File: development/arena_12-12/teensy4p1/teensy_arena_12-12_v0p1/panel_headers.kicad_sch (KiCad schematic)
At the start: 27 parts, among them P1 CONN15, P10 CONN15, P11 CONN15, P12 CONN15, P2 CONN15, P3 CONN15, P4 CONN15, P5 CONN15, P6 CONN15, P7 CONN15, P8 CONN15, P9 CONN15, Q2 MOSFET_NCHAN

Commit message: Worked on 12-12 teensy4p1 arena without vreg.
Modified SPI connections from teensy to panel columns so that all
signals go from a single source to a single destinatin. Also, added
source termination resistors and schmitt trigger buffers to all SPI
signals.
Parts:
- added C100, C101, C102, C103, C104, C105, C106, C107, C108, C109, C110, C111, C112, C113, C114, C115, C116, C117, C118, C119, C120, C121, C122, C123, C124, C125, C126, C127, C128, C129, C130, C131, C132, C133, C134, C135, C136, C137, C138, C139, C140, C141, C142, C143, C144, C145, C146, C147, C148, C149, C150, C151, C152, C153, C154, C155, C156, C157, C158, C159, C160, C161, C162, C163, C164, C165, C166, C167, C168, C169, C170, C171, C172, C77, C78, C79, C80, C81, C82, C83, C84, C85, C86, C87, C88, C89, C90, C91, C92, C93, C94, C95, C96, C97, C98, C99: 0.1uF, Capacitor_SMD:C_0603_1608Metric, symbol Device:C
- added R127, R128, R129, R130, R131, R132, R133, R134, R135, R136, R137, R138, R139, R140, R141, R142, R143, R144, R145, R146, R147, R148, R149, R150, R151, R152, R153, R154, R155, R156, R157, R158, R159, R160, R161, R162, R163, R164, R165, R166, R167, R168, R169, R170, R171, R172, R173, R174, R175, R176, R177, R178, R179, R180, R181, R182, R183, R184, R185, R186, R187, R188, R189, R190, R191, R192, R193, R194, R195, R196, R197, R198, R199, R200, R201, R202, R203, R204, R205, R206, R207, R208, R209, R210, R211, R212, R213, R214, R215, R216, R217, R218, R219, R220, R221, R222: 68, symbol Device:R
- added U100, U101, U102, U103, U104, U105, U106, U107, U108, U109, U110, U111, U112, U113, U114, U115, U116, U117, U118, U119, U120, U121, U122, U123, U124, U125, U126, U127, U128, U129, U130, U131, U132, U133, U134, U135, U136, U137, U138, U139, U140, U141, U142, U143, U144, U145, U146, U147, U148, U149, U54, U55, U56, U57, U58, U59, U60, U61, U62, U63, U64, U65, U66, U67, U68, U69, U70, U71, U72, U73, U74, U75, U76, U77, U78, U79, U80, U81, U82, U83, U84, U85, U86, U87, U88, U89, U90, U91, U92, U93, U94, U95, U96, U97, U98, U99: 74LVC1G17, symbol 74xGxx:74LVC1G17
- Q2: footprint Package_TO_SOT_SMD:SOT-23-3 -> (none)
- renumbered C11 to C65, C12 to C66, C13 to C67, C14 to C68, C15 to C69, C16 to C70, C17 to C71, C18 to C72, C19 to C73, C20 to C74, C21 to C75, C22 to C76
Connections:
- net +5V: now also C100.1, C101.1, C102.1, C103.1, C104.1, C105.1, C106.1, C107.1, C108.1, C109.1, C110.1, C111.1, C112.1, C113.1, C114.1, C115.1, C116.1, C117.1, C118.1, C119.1, C120.1, C121.1, C122.1, C123.1, C124.1, C125.1, C126.1, C127.1, C128.1, C129.1, C130.1, C131.1, C132.1, C133.1, C134.1, C135.1, C136.1, C137.1, C138.1, C139.1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
- net GND: now also C100.2, C101.2, C102.2, C103.2, C104.2, C105.2, C106.2, C107.2, C108.2, C109.2, C110.2, C111.2, C112.2, C113.2, C114.2, C115.2, C116.2, C117.2, C118.2, C119.2, C120.2, C121.2, C122.2, C123.2, C124.2, C125.2, C126.2, C127.2, C128.2, C129.2, C130.2, C131.2, C132.2, C133.2, C134.2, C135.2, C136.2, C137.2, C138.2, C139.2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
- net PAN5V.EXT_INT: now also U101.2, U109.2, U117.2, U125.2, U133.2, U141.2, U149.2, U61.2, U69.2, U77.2, U85.2, U93.2; no longer P1.15, P10.15, P11.15, P12.15, P2.15, P3.15, P4.15, P5.15, P6.15, P7.15, P8.15, P9.15
- net PAN5V.MISO_0: no longer P4.6
- net PAN5V.CS_00 renamed HDR_CS_00_P1
- net HDR_CS_00_P1: now also R129.1; no longer P7.7
- net PAN5V.CS_01 renamed HDR_CS_01_P1
- net HDR_CS_01_P1: now also R130.1; no longer P7.8
- net PAN5V.CS_02 renamed HDR_CS_02_P1
- net HDR_CS_02_P1: now also R131.1; no longer P7.9
- net PAN5V.CS_03 renamed HDR_CS_03_P1
- net HDR_CS_03_P1: now also R132.1; no longer P7.10
- net PAN5V.CS_04 renamed HDR_CS_04_P1
- net HDR_CS_04_P1: now also R133.1; no longer P7.11
- net PAN5V.CS_05 renamed HDR_CS_05_P2
- net HDR_CS_05_P2: now also R137.1; no longer P8.7
- net PAN5V.CS_06 renamed HDR_CS_06_P2
- net HDR_CS_06_P2: now also R138.1; no longer P8.8
- net PAN5V.CS_07 renamed HDR_CS_07_P2
- net HDR_CS_07_P2: now also R139.1; no longer P8.9
- net PAN5V.CS_08 renamed HDR_CS_08_P2
- net HDR_CS_08_P2: now also R140.1; no longer P8.10
- net PAN5V.CS_09 renamed HDR_CS_09_P2
- net HDR_CS_09_P2: now also R141.1; no longer P8.11
- net PAN5V.CS_10 renamed HDR_CS_10_P3
- net HDR_CS_10_P3: now also R145.1; no longer P9.7
- net PAN5V.CS_11 renamed HDR_CS_11_P3
- net HDR_CS_11_P3: now also R146.1; no longer P9.8
- net PAN5V.CS_12 renamed HDR_CS_12_P3
- net HDR_CS_12_P3: now also R147.1; no longer P9.9
- net PAN5V.CS_13 renamed HDR_CS_13_P3
- net HDR_CS_13_P3: now also R148.1; no longer P9.10
- net PAN5V.CS_14 renamed HDR_CS_14_P3
- net HDR_CS_14_P3: now also R149.1; no longer P9.11
- net PAN5V.CS_15 renamed HDR_CS_15_P10
- net HDR_CS_15_P10: now also R201.1; no longer P4.7
- net PAN5V.CS_16 renamed HDR_CS_16_P10
- net HDR_CS_16_P10: now also R202.1; no longer P4.8
- net PAN5V.CS_17 renamed HDR_CS_17_P10
- net HDR_CS_17_P10: now also R203.1; no longer P4.9
- net PAN5V.CS_18 renamed HDR_CS_18_P10
- net HDR_CS_18_P10: now also R204.1; no longer P4.10
- net PAN5V.CS_19 renamed HDR_CS_19_P10
- net HDR_CS_19_P10: now also R205.1; no longer P4.11
- net PAN5V.CS_20 renamed HDR_CS_20_P11
- net HDR_CS_20_P11: now also R209.1; no longer P5.7
- net PAN5V.CS_21 renamed HDR_CS_21_P11
- net HDR_CS_21_P11: now also R210.1; no longer P5.8
- net PAN5V.CS_22 renamed HDR_CS_22_P11
- net HDR_CS_22_P11: now also R211.1; no longer P5.9
- net PAN5V.CS_23 renamed HDR_CS_23_P11
- net HDR_CS_23_P11: now also R212.1; no longer P5.10
- net PAN5V.CS_24 renamed HDR_CS_24_P11
- net HDR_CS_24_P11: now also R213.1; no longer P5.11
- net PAN5V.CS_25 renamed HDR_CS_25_P12
- net HDR_CS_25_P12: now also R217.1; no longer P6.7
- net PAN5V.CS_26 renamed HDR_CS_26_P12
- net HDR_CS_26_P12: now also R218.1; no longer P6.8
- net PAN5V.CS_27 renamed HDR_CS_27_P12
- net HDR_CS_27_P12: now also R219.1; no longer P6.9
- net PAN5V.CS_28 renamed HDR_CS_28_P12
- net HDR_CS_28_P12: now also R220.1; no longer P6.10
- net PAN5V.CS_29 renamed HDR_CS_29_P12
- net HDR_CS_29_P12: now also R221.1; no longer P6.11
- removed net PAN5V.MOSI_0: P1.5, P2.5, P3.5, P4.5, P5.5, P6.5
- removed net PAN5V.MOSI_1: P10.5, P11.5, P12.5, P7.5, P8.5, P9.5
- removed net PAN5V.SCK_0: P1.4, P2.4, P3.4, P4.4, P5.4, P6.4
- removed net PAN5V.SCK_1: P10.4, P11.4, P12.4, P7.4, P8.4, P9.4
- net RESET renamed HDR_RESET
- new net: R195.2, U122.4
- new net: R200.2, U127.4
- new net: R140.2, U67.4
- new net: R177.2, U104.4
- new net: R136.2, U63.4
- new net: R158.2, U85.4
- new net: R181.2, U108.4
- new net: R152.2, U79.4
- new net: R144.2, U71.4
- new net: R154.2, U81.4
- new net: R217.2, U144.4
- new net: R220.2, U147.4
- new net: R130.2, U57.4
- new net: R201.2, U128.4
- new net: R213.2, U140.4
- new net: R196.2, U123.4
- new net: R168.2, U95.4
- new net: R185.2, U112.4
- new net: R178.2, U105.4
- new net: R183.2, U110.4
- new net: R199.2, U126.4
- new net: R173.2, U100.4
- new net: R188.2, U115.4
- new net: R164.2, U91.4
- new net: R170.2, U97.4
- new net: R212.2, U139.4
- new net: R133.2, U60.4
- new net: R155.2, U82.4
- new net: R207.2, U134.4
- new net: R127.2, U54.4
- new net: R159.2, U86.4
- new net: R179.2, U106.4
- new net: R194.2, U121.4
- new net: R190.2, U117.4
- new net: R138.2, U65.4
- new net: R202.2, U129.4
- new net: R182.2, U109.4
- new net: R163.2, U90.4
- new net: R187.2, U114.4
- new net: R222.2, U149.4
- new net: R148.2, U75.4
- new net: R208.2, U135.4
- new net: R198.2, U125.4
- new net: R142.2, U69.4
- new net: R192.2, U119.4
- new net: R132.2, U59.4
- new net: R206.2, U133.4
- new net: R180.2, U107.4
- new net: R145.2, U72.4
- new net: R167.2, U94.4
- new net: R141.2, U68.4
- new net: R156.2, U83.4
- new net: R204.2, U131.4
- new net: R214.2, U141.4
- new net: R197.2, U124.4
- new net: R135.2, U62.4
- new net: R171.2, U98.4
- new net: R215.2, U142.4
- new net: R131.2, U58.4
- new net: R176.2, U103.4
- new net: R139.2, U66.4
- new net: R174.2, U101.4
- new net: R209.2, U136.4
- new net: R219.2, U146.4
- new net: R175.2, U102.4
- new net: R203.2, U130.4
- new net: R193.2, U120.4
- new net: R149.2, U76.4
- new net: R134.2, U61.4
- new net: R165.2, U92.4
- new net: R137.2, U64.4
- new net: R172.2, U99.4
- new net: R151.2, U78.4
- new net: R218.2, U145.4
- new net: R210.2, U137.4
- new net: R128.2, U55.4
- new net: R162.2, U89.4
- new net: R146.2, U73.4
- new net: R221.2, U148.4
- new net: R150.2, U77.4
- new net: R184.2, U111.4
- new net: R153.2, U80.4
- new net: R169.2, U96.4
- new net: R147.2, U74.4
- new net: R191.2, U118.4
- new net: R189.2, U116.4
- new net: R160.2, U87.4
- new net: R216.2, U143.4
- new net: R129.2, U56.4
- new net: R205.2, U132.4
- new net: R143.2, U70.4
- new net: R157.2, U84.4
- new net: R186.2, U113.4
- new net: R211.2, U138.4
- new net: R161.2, U88.4
- new net: R166.2, U93.4
- new net HDR_CS_00_P7: P7.7, R177.1
- new net HDR_CS_01_P7: P7.8, R178.1
- new net HDR_CS_02_P7: P7.9, R179.1
- new net HDR_CS_03_P7: P7.10, R180.1
- new net HDR_CS_04_P7: P7.11, R181.1
- new net HDR_CS_05_P8: P8.7, R185.1
- new net HDR_CS_06_P8: P8.8, R186.1
- new net HDR_CS_07_P8: P8.9, R187.1
- new net HDR_CS_08_P8: P8.10, R188.1
- new net HDR_CS_09_P8: P8.11, R189.1
- new net HDR_CS_10_P9: P9.7, R193.1
- new net HDR_CS_11_P9: P9.8, R194.1
- new net HDR_CS_12_P9: P9.9, R195.1
- new net HDR_CS_13_P9: P9.10, R196.1
- new net HDR_CS_14_P9: P9.11, R197.1
- new net HDR_CS_15_P4: P4.7, R153.1
- new net HDR_CS_16_P4: P4.8, R154.1
- new net HDR_CS_17_P4: P4.9, R155.1
- new net HDR_CS_18_P4: P4.10, R156.1
- new net HDR_CS_19_P4: P4.11, R157.1
- new net HDR_CS_20_P5: P5.7, R161.1
- new net HDR_CS_21_P5: P5.8, R162.1
- new net HDR_CS_22_P5: P5.9, R163.1
- new net HDR_CS_23_P5: P5.10, R164.1
- new net HDR_CS_24_P5: P5.11, R165.1
- new net HDR_CS_25_P6: P6.7, R169.1
- new net HDR_CS_26_P6: P6.8, R170.1
- new net HDR_CS_27_P6: P6.9, R171.1
- new net HDR_CS_28_P6: P6.10, R172.1
- new net HDR_CS_29_P6: P6.11, R173.1
- new net HDR_EXT_INT_P1: P1.15, R134.1
- new net HDR_EXT_INT_P10: P10.15, R206.1
- new net HDR_EXT_INT_P11: P11.15, R214.1
- new net HDR_EXT_INT_P12: P12.15, R222.1
- new net HDR_EXT_INT_P2: P2.15, R142.1
- new net HDR_EXT_INT_P3: P3.15, R150.1
- new net HDR_EXT_INT_P4: P4.15, R158.1
- new net HDR_EXT_INT_P5: P5.15, R166.1
- new net HDR_EXT_INT_P6: P6.15, R174.1
- new net HDR_EXT_INT_P7: P7.15, R182.1
- new net HDR_EXT_INT_P8: P8.15, R190.1
- new net HDR_EXT_INT_P9: P9.15, R198.1
- new net HDR_MISO_0: P4.6
- new net HDR_MOSI_0_P1: P1.5, R128.1
- new net HDR_MOSI_0_P2: P2.5, R136.1
- new net HDR_MOSI_0_P3: P3.5, R144.1
- new net HDR_MOSI_0_P4: R152.1
- new net HDR_MOSI_0_P5: P5.5, R160.1
- new net HDR_MOSI_0_P6: P6.5, R168.1
- new net HDR_MOSI_1_P10: P10.5, R200.1
- new net HDR_MOSI_1_P11: P11.5, R208.1
- new net HDR_MOSI_1_P12: P12.5, R216.1
- new net HDR_MOSI_1_P7: P7.5, R176.1
- new net HDR_MOSI_1_P8: P8.5, R184.1
- new net HDR_MOSI_1_P9: P9.5, R192.1
- new net HDR_SCK_0_P1: P1.4, R127.1
- new net HDR_SCK_0_P2: P2.4, R135.1
- new net HDR_SCK_0_P3: P3.4, R143.1
- new net HDR_SCK_0_P4: P4.4, R151.1
- new net HDR_SCK_0_P5: P5.4, R159.1
- new net HDR_SCK_0_P6: P6.4, R167.1
- new net HDR_SCK_1_P10: P10.4, R199.1
- new net HDR_SCK_1_P11: P11.4, R207.1
- new net HDR_SCK_1_P12: P12.4, R215.1
- new net HDR_SCK_1_P7: P7.4, R175.1
- new net HDR_SCK_1_P8: P8.4, R183.1
- new net HDR_SCK_1_P9: P9.4, R191.1
- new net PAN5V.CS_00_P1: U56.2
- new net PAN5V.CS_00_P7: U104.2
- new net PAN5V.CS_01_P1: U57.2
- new net PAN5V.CS_01_P7: U105.2
- new net PAN5V.CS_02_P1: U58.2
- new net PAN5V.CS_02_P7: U106.2
- new net PAN5V.CS_03_P1: U59.2
- new net PAN5V.CS_03_P7: U107.2
- new net PAN5V.CS_04_P1: U60.2
- new net PAN5V.CS_04_P7: U108.2
- new net PAN5V.CS_05_P2: U64.2
- new net PAN5V.CS_05_P8: U112.2
- new net PAN5V.CS_06_P2: U65.2
- new net PAN5V.CS_06_P8: U113.2
- new net PAN5V.CS_07_P2: U66.2
- new net PAN5V.CS_07_P8: U114.2
- new net PAN5V.CS_08_P2: U67.2
- new net PAN5V.CS_08_P8: U115.2
- new net PAN5V.CS_09_P2: U68.2
- new net PAN5V.CS_09_P8: U116.2
- new net PAN5V.CS_10_P3: U72.2
- new net PAN5V.CS_10_P9: U120.2
- new net PAN5V.CS_11_P3: U73.2
- new net PAN5V.CS_11_P9: U121.2
- new net PAN5V.CS_12_P3: U74.2
- new net PAN5V.CS_12_P9: U122.2
- new net PAN5V.CS_13_P3: U75.2
- new net PAN5V.CS_13_P9: U123.2
- new net PAN5V.CS_14_P3: U76.2
- new net PAN5V.CS_14_P9: U124.2
- new net PAN5V.CS_15_P10: U128.2
- new net PAN5V.CS_15_P4: U80.2
- new net PAN5V.CS_16_P10: U129.2
- new net PAN5V.CS_16_P4: U81.2
- new net PAN5V.CS_17_P10: U130.2
- new net PAN5V.CS_17_P4: U82.2
- new net PAN5V.CS_18_P10: U131.2
- new net PAN5V.CS_18_P4: U83.2
- new net PAN5V.CS_19_P10: U132.2
- new net PAN5V.CS_19_P4: U84.2
- new net PAN5V.CS_20_P11: U136.2
- new net PAN5V.CS_20_P5: U88.2
- new net PAN5V.CS_21_P11: U137.2
- new net PAN5V.CS_21_P5: U89.2
- new net PAN5V.CS_22_P11: U138.2
- new net PAN5V.CS_22_P5: U90.2
- new net PAN5V.CS_23_P11: U139.2
- new net PAN5V.CS_23_P5: U91.2
- new net PAN5V.CS_24_P11: U140.2
- new net PAN5V.CS_24_P5: U92.2
- new net PAN5V.CS_25_P12: U144.2
- new net PAN5V.CS_25_P6: U96.2
- new net PAN5V.CS_26_P12: U145.2
- new net PAN5V.CS_26_P6: U97.2
- new net PAN5V.CS_27_P12: U146.2
- new net PAN5V.CS_27_P6: U98.2
- new net PAN5V.CS_28_P12: U147.2
- new net PAN5V.CS_28_P6: U99.2
- new net PAN5V.CS_29_P12: U148.2
- new net PAN5V.CS_29_P6: U100.2
- new net PAN5V.MOSI_0_P1: U55.2
- new net PAN5V.MOSI_0_P2: U63.2
- new net PAN5V.MOSI_0_P3: U71.2
- new net PAN5V.MOSI_0_P4: P4.5, U79.2
- new net PAN5V.MOSI_0_P5: U87.2
- new net PAN5V.MOSI_0_P6: U95.2
- new net PAN5V.MOSI_1_P10: U127.2
- new net PAN5V.MOSI_1_P11: U135.2
- new net PAN5V.MOSI_1_P12: U143.2
- new net PAN5V.MOSI_1_P7: U103.2
- new net PAN5V.MOSI_1_P8: U111.2
- new net PAN5V.MOSI_1_P9: U119.2
- new net PAN5V.SCK_0_P1: U54.2
- new net PAN5V.SCK_0_P2: U62.2
- new net PAN5V.SCK_0_P3: U70.2
- new net PAN5V.SCK_0_P4: U78.2
- new net PAN5V.SCK_0_P5: U86.2
- new net PAN5V.SCK_0_P6: U94.2
- new net PAN5V.SCK_1_P10: U126.2
- new net PAN5V.SCK_1_P11: U134.2
- new net PAN5V.SCK_1_P12: U142.2
- new net PAN5V.SCK_1_P7: U102.2
- new net PAN5V.SCK_1_P8: U110.2
- new net PAN5V.SCK_1_P9: U118.2
- no-connect marks 36 -> 132
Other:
- moved on the sheet: C65, C66, C67, C68, C69, C70, C71, C72, C73, C74, C75, C76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

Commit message: More work on schematic for 12-12 teensy arena.
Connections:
- net HDR_MISO_0 is gone; now on net PAN5V.MISO_0: P4.6
- net HDR_MOSI_0_P4: now also P4.5
- net PAN5V.MOSI_0_P4: no longer P4.5
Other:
- moved on the sheet: C68, C73, R1, R2

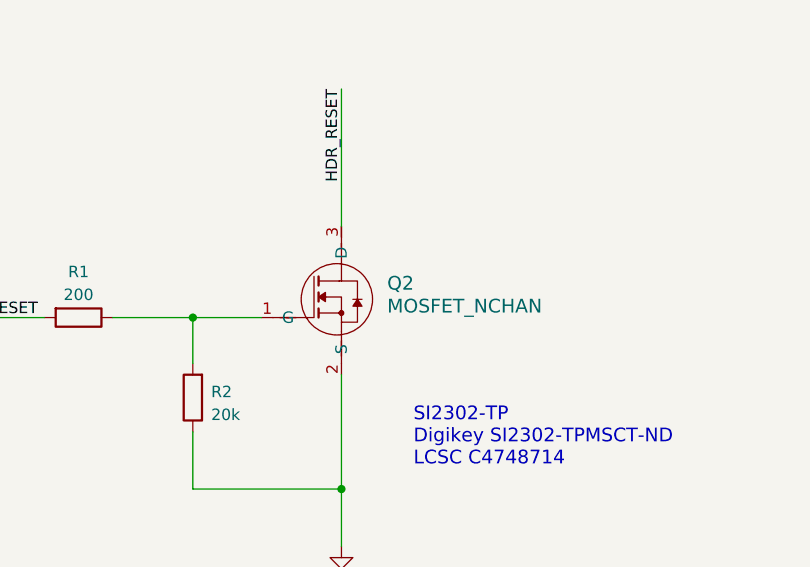
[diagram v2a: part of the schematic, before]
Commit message: Reworked schematic for 12-12 teensy arena w/o regulators some more.
Worked on foot print assignmets. Started replacing some of the single
schmitt triggers with equivalent dual versions to reduce component
count.
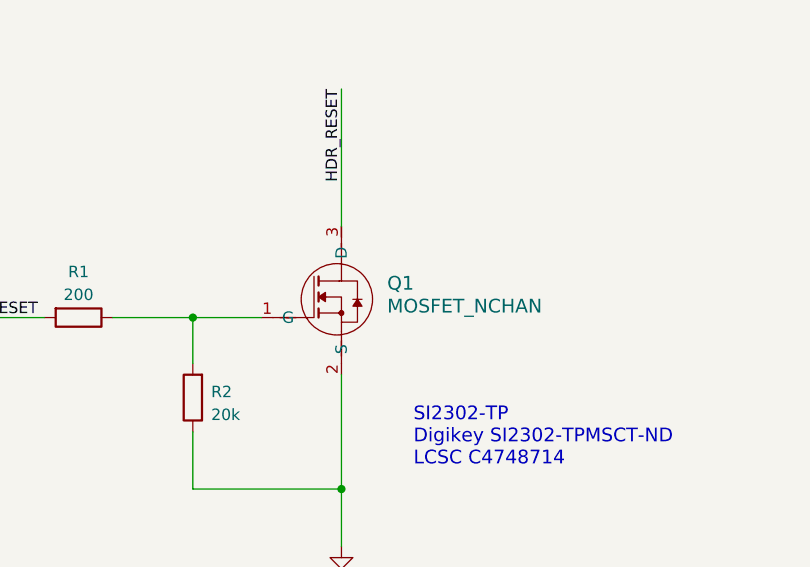
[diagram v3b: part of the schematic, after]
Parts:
- Q1: renamed from Q2; footprint (none) -> Package_TO_SOT_SMD:SOT-23-3
- R127, R128, R129, R130, R131, R132, R133, R134, R135, R136, R137, R138, R139, R140, R141, R142, R143, R144, R145, R146, R147, R148, R149, R150, R151, R152, R153, R154, R155, R156, R157, R158, R159, R160, R161, R162, R163, R164, R165, R166, R167, R168, R169, R170, R171, R172, R173, R174, R175, R176, R177, R178, R179, R180, R181, R182, R183, R184, R185, R186, R187, R188, R189, R190, R191, R192, R193, R194, R195, R196, R197, R198, R199, R200, R201, R202, R203, R204, R205, R206, R207, R208, R209, R210, R211, R212, R213, R214, R215, R216, R217, R218, R219, R220, R221, R222: footprint (none) -> Resistor_SMD:R_0603_1608Metric

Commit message: Finished initial schematic for 12-12 teensy 4.1 arena w/o vreg.
Finished footprint assignments and started working on layout changes.
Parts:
- removed C100, C101, C102, C103, C104, C105, C106, C107, C108, C109, C110, C111, C112, C113, C114, C115, C116, C117, C118, C119, C120, C121, C122, C123, C124, C125, C126, C127, C128, C129, C130, C131, C132, C133, C134, C135, C136, C137, C138, C139, C140, C141, C142, C143, C144, C145, C146, C147, C148, C149, C150, C151, C152, C153, C154, C155, C156, C157, C158, C159, C160, C161, C162, C163, C164, C165, C166, C167, C168, C169, C170, C171, C172, C95, C96, C97, C98, C99: 0.1uF, Capacitor_SMD:C_0603_1608Metric, symbol Device:C
- removed U100, U101, U102, U103, U104, U105, U106, U107, U108, U109, U110, U111, U112, U113, U114, U115, U116, U117, U118, U119, U120, U121, U122, U123, U124, U125, U126, U127, U128, U129, U130, U131, U132, U133, U134, U135, U136, U137, U138, U139, U140, U141, U142, U143, U144, U145, U146, U147, U148, U149, U54, U55, U56, U57, U58, U59, U60, U61, U62, U63, U64, U65, U66, U67, U68, U69, U70, U71, U72, U73, U74, U75, U76, U77, U78, U79, U80, U81, U82, U83, U84, U85, U86, U87, U88, U89, U90, U91, U92, U93, U94, U95, U96, U97, U98, U99: 74LVC1G17, symbol 74xGxx:74LVC1G17
- added C47, C48, C49, C50, C51, C52, C53, C54, C55, C56, C57, C58, C59, C60, C61, C62, C63, C64, C65, C66, C67, C68, C69, C70, C71, C72, C73, C74, C75, C76: 0.1uF, Capacitor_SMD:C_0603_1608Metric, symbol Device:C
- added U36, U37, U38, U39, U40, U41, U42, U43, U44, U45, U46, U47, U48, U49, U50, U51, U52, U53, U54, U55, U56, U57, U58, U59, U60, U61, U62, U63, U64, U65, U66, U67, U68, U69, U70, U71, U72, U73, U74, U75, U76, U77, U78, U79, U80, U81, U82, U83: 74LVC2G17, Package_TO_SOT_SMD:SOT-23-6, symbol 74xGxx:74LVC2G17
- renumbered C70 to C100, C71 to C101, C72 to C102, C73 to C103, C74 to C104, C75 to C105, C76 to C106, C65 to C95, C66 to C96, C67 to C97, C68 to C98, C69 to C99
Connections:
- net +5V: no longer C77.1, C78.1, C79.1, C80.1, C81.1, C82.1, C83.1, C84.1, C85.1, C86.1, C87.1, C88.1, C89.1, C90.1, C91.1, C92.1, C93.1, C94.1
- net GND: now also C47.2, C48.2, C49.2, C50.2, C51.2, C52.2, C53.2, C54.2, C55.2, C56.2, C57.2, C58.2, C59.2, C60.2, C61.2, C62.2, C63.2, C64.2, C65.2, C66.2, C67.2, C68.2, C69.2, C70.2, C71.2, C72.2, C73.2, C74.2, C75.2, C76.2, U36.2 (GND), U37.2 (GND), U38.2 (GND), U39.2 (GND), U40.2 (GND), U41.2 (GND), U42.2 (GND), U43.2 (GND), U44.2 (GND), U45.2 (GND), U46.2 (GND), U47.2 (GND), U48.2 (GND), U49.2 (GND), U50.2 (GND), U51.2 (GND), U52.2 (GND), U53.2 (GND), U54.2 (GND), U55.2 (GND), U56.2 (GND), U57.2 (GND), U58.2 (GND), U59.2 (GND), U60.2 (GND), U61.2 (GND), U62.2 (GND), U63.2 (GND), U64.2 (GND), U65.2 (GND), U66.2 (GND), U67.2 (GND), U68.2 (GND), U69.2 (GND), U70.2 (GND), U71.2 (GND), U72.2 (GND), U73.2 (GND), U74.2 (GND), U75.2 (GND), U76.2 (GND), U77.2 (GND), U78.2 (GND), U79.2 (GND), U80.2 (GND), U81.2 (GND), U82.2 (GND), U83.2 (GND)
- net PAN5V.CS_00_P1: now also U37.1
- net PAN5V.CS_00_P7: now also U61.1
- net PAN5V.CS_01_P1: now also U37.3
- net PAN5V.CS_01_P7: now also U61.3
- net PAN5V.CS_02_P1: now also U38.1
- net PAN5V.CS_02_P7: now also U62.1
- net PAN5V.CS_03_P1: now also U38.3
- net PAN5V.CS_03_P7: now also U62.3
- net PAN5V.CS_04_P1: now also U39.1
- net PAN5V.CS_04_P7: now also U63.1
- net PAN5V.CS_05_P2: now also U41.1
- net PAN5V.CS_05_P8: now also U65.1
- net PAN5V.CS_06_P2: now also U41.3
- net PAN5V.CS_06_P8: now also U65.3
- net PAN5V.CS_07_P2: now also U42.1
- net PAN5V.CS_07_P8: now also U66.1
- net PAN5V.CS_08_P2: now also U42.3
- net PAN5V.CS_08_P8: now also U66.3
- net PAN5V.CS_09_P2: now also U43.1
- net PAN5V.CS_09_P8: now also U67.1
- net PAN5V.CS_10_P3: now also U45.1
- net PAN5V.CS_10_P9: now also U69.1
- net PAN5V.CS_11_P3: now also U45.3
- net PAN5V.CS_11_P9: now also U69.3
- net PAN5V.CS_12_P3: now also U46.1
- net PAN5V.CS_12_P9: now also U70.1
- net PAN5V.CS_13_P3: now also U46.3
- net PAN5V.CS_13_P9: now also U70.3
- net PAN5V.CS_14_P3: now also U47.1
- net PAN5V.CS_14_P9: now also U71.1
- net PAN5V.CS_15_P10: now also U73.1
- net PAN5V.CS_15_P4: now also U49.1
- net PAN5V.CS_16_P10: now also U73.3
- net PAN5V.CS_16_P4: now also U49.3
- net PAN5V.CS_17_P10: now also U74.1
- net PAN5V.CS_17_P4: now also U50.1
- net PAN5V.CS_18_P10: now also U74.3
- net PAN5V.CS_18_P4: now also U50.3
- net PAN5V.CS_19_P10: now also U75.1
- net PAN5V.CS_19_P4: now also U51.1
- net PAN5V.CS_20_P11: now also U77.1
- net PAN5V.CS_20_P5: now also U53.1
- net PAN5V.CS_21_P11: now also U77.3
- net PAN5V.CS_21_P5: now also U53.3
- net PAN5V.CS_22_P11: now also U78.1
- net PAN5V.CS_22_P5: now also U54.1
- net PAN5V.CS_23_P11: now also U78.3
- net PAN5V.CS_23_P5: now also U54.3
- net PAN5V.CS_24_P11: now also U79.1
- net PAN5V.CS_24_P5: now also U55.1
- net PAN5V.CS_25_P12: now also U81.1
- net PAN5V.CS_25_P6: now also U57.1
- net PAN5V.CS_26_P12: now also U81.3
- net PAN5V.CS_26_P6: now also U57.3
- net PAN5V.CS_27_P12: now also U82.1
- net PAN5V.CS_27_P6: now also U58.1
- net PAN5V.CS_28_P12: now also U82.3
- net PAN5V.CS_28_P6: now also U58.3
- net PAN5V.CS_29_P12: now also U83.1
- net PAN5V.CS_29_P6: now also U59.1
- net PAN5V.EXT_INT: now also U39.3, U43.3, U47.3, U51.3, U55.3, U59.3, U63.3, U67.3, U71.3, U75.3, U79.3, U83.3
- net PAN5V.MOSI_0_P1: now also U36.3
- net PAN5V.MOSI_0_P2: now also U40.3
- net PAN5V.MOSI_0_P3: now also U44.3
- net PAN5V.MOSI_0_P4: now also U48.3
- net PAN5V.MOSI_0_P5: now also U52.3
- net PAN5V.MOSI_0_P6: now also U56.3
- net PAN5V.MOSI_1_P10: now also U72.3
- net PAN5V.MOSI_1_P11: now also U76.3
- net PAN5V.MOSI_1_P12: now also U80.3
- net PAN5V.MOSI_1_P7: now also U60.3
- net PAN5V.MOSI_1_P8: now also U64.3
- net PAN5V.MOSI_1_P9: now also U68.3
- net PAN5V.SCK_0_P1: now also U36.1
- net PAN5V.SCK_0_P2: now also U40.1
- net PAN5V.SCK_0_P3: now also U44.1
- net PAN5V.SCK_0_P4: now also U48.1
- net PAN5V.SCK_0_P5: now also U52.1
- net PAN5V.SCK_0_P6: now also U56.1
- net PAN5V.SCK_1_P10: now also U72.1
- net PAN5V.SCK_1_P11: now also U76.1
- net PAN5V.SCK_1_P12: now also U80.1
- net PAN5V.SCK_1_P7: now also U60.1
- net PAN5V.SCK_1_P8: now also U64.1
- net PAN5V.SCK_1_P9: now also U68.1
- net at R195.2: now also U70.6
- net at R200.2: now also U72.4
- net at R140.2: now also U42.4
- net at R177.2: now also U61.6
- net at R136.2: now also U40.4
- net at R158.2: now also U51.4
- net at R181.2: now also U63.6
- net at R152.2: now also U48.4
- net at R144.2: now also U44.4
- net at R154.2: now also U49.4
- net at R217.2: now also U81.6
- net at R220.2: now also U82.4
- net at R130.2: now also U37.4
- net at R201.2: now also U73.6
- net at R213.2: now also U79.6
- net at R196.2: now also U70.4
- net at R168.2: now also U56.4
- net at R185.2: now also U65.6
- net at R178.2: now also U61.4
- net at R183.2: now also U64.6
- net at R199.2: now also U72.6
- net at R173.2: now also U59.6
- net at R188.2: now also U66.4
- net at R164.2: now also U54.4
- net at R170.2: now also U57.4
- net at R212.2: now also U78.4
- net at R133.2: now also U39.6
- net at R155.2: now also U50.6
- net at R207.2: now also U76.6
- net at R127.2: now also U36.6
- net at R159.2: now also U52.6
- net at R179.2: now also U62.6
- net at R194.2: now also U69.4
- net at R190.2: now also U67.4
- net at R138.2: now also U41.4
- net at R202.2: now also U73.4
- net at R182.2: now also U63.4
- net at R163.2: now also U54.6
- net at R187.2: now also U66.6
- net at R222.2: now also U83.4
- net at R148.2: now also U46.4
- net at R208.2: now also U76.4
- net at R198.2: now also U71.4
- net at R142.2: now also U43.4
- net at R192.2: now also U68.4
- net at R132.2: now also U38.4
- net at R206.2: now also U75.4
- net at R180.2: now also U62.4
- net at R145.2: now also U45.6
- net at R167.2: now also U56.6
- net at R141.2: now also U43.6
- net at R156.2: now also U50.4
- net at R204.2: now also U74.4
- net at R214.2: now also U79.4
- net at R197.2: now also U71.6
- net at R135.2: now also U40.6
- net at R171.2: now also U58.6
- net at R215.2: now also U80.6
- net at R131.2: now also U38.6
- net at R176.2: now also U60.4
- net at R139.2: now also U42.6
- net at R174.2: now also U59.4
- net at R209.2: now also U77.6
- net at R219.2: now also U82.6
- net at R175.2: now also U60.6
- net at R203.2: now also U74.6
- net at R193.2: now also U69.6
- net at R149.2: now also U47.6
- net at R134.2: now also U39.4
- net at R165.2: now also U55.6
- net at R137.2: now also U41.6
- net at R172.2: now also U58.4
- net at R151.2: now also U48.6
- net at R218.2: now also U81.4
- net at R210.2: now also U77.4
- net at R128.2: now also U36.4
- net at R162.2: now also U53.4
- net at R146.2: now also U45.4
- net at R221.2: now also U83.6
- net at R150.2: now also U47.4
- net at R184.2: now also U64.4
- net at R153.2: now also U49.6
- net at R169.2: now also U57.6
- net at R147.2: now also U46.6
- net at R191.2: now also U68.6
- net at R189.2: now also U67.6
- net at R160.2: now also U52.4
- net at R216.2: now also U80.4
- net at R129.2: now also U37.6
- net at R205.2: now also U75.6
- net at R143.2: now also U44.6
- net at R157.2: now also U51.6
- net at R186.2: now also U65.4
- net at R211.2: now also U78.6
- net at R161.2: now also U53.6
- net at R166.2: now also U55.4
- new net +3.3V: C47.1, C48.1, C49.1, C50.1, C51.1, C52.1, C53.1, C54.1, C55.1, C56.1, C57.1, C58.1, C59.1, C60.1, C61.1, C62.1, C63.1, C64.1, C65.1, C66.1, C67.1, C68.1, C69.1, C70.1, C71.1, C72.1, C73.1, C74.1, C75.1, C76.1, C77.1, C78.1, C79.1, C80.1, C81.1, C82.1, C83.1, C84.1, C85.1, C86.1, C87.1, C88.1, C89.1, C90.1, C91.1, C92.1, C93.1, C94.1, U36.5 (VCC), U37.5 (VCC), U38.5 (VCC), U39.5 (VCC), U40.5 (VCC), U41.5 (VCC), U42.5 (VCC), U43.5 (VCC), U44.5 (VCC), U45.5 (VCC), U46.5 (VCC), U47.5 (VCC), U48.5 (VCC), U49.5 (VCC), U50.5 (VCC), U51.5 (VCC), U52.5 (VCC), U53.5 (VCC), U54.5 (VCC), U55.5 (VCC), U56.5 (VCC), U57.5 (VCC), U58.5 (VCC), U59.5 (VCC), U60.5 (VCC), U61.5 (VCC), U62.5 (VCC), U63.5 (VCC), U64.5 (VCC), U65.5 (VCC), U66.5 (VCC), U67.5 (VCC), U68.5 (VCC), U69.5 (VCC), U70.5 (VCC), U71.5 (VCC), U72.5 (VCC), U73.5 (VCC), U74.5 (VCC), U75.5 (VCC), U76.5 (VCC), U77.5 (VCC), U78.5 (VCC), U79.5 (VCC), U80.5 (VCC), U81.5 (VCC), U82.5 (VCC), U83.5 (VCC)
- no-connect marks 132 -> 36
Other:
- note added: "Swap A and B units for better routing?"
- moved on the sheet: R128, R130, R132, R134, R136, R138, R140, R142, R144, R146, R148, R150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

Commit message: Added source termination resistors to miso lines.
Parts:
- added R223, R224, R225, R226, R227, R228, R229, R230, R231, R232, R233, R234: 68, Resistor_SMD:R_0603_1608Metric, symbol Device:R
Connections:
- net PAN5V.MISO_0: now also R223.2, R224.2, R225.2, R226.2, R227.2, R228.2; no longer P1.6, P2.6, P3.6, P4.6, P5.6, P6.6
- net PAN5V.MISO_1: now also R229.2, R230.2, R231.2, R232.2, R233.2, R234.2; no longer P10.6, P11.6, P12.6, P7.6, P8.6, P9.6
- new net HDR_MISO_0_P1: P1.6, R223.1
- new net HDR_MISO_0_P2: P2.6, R224.1
- new net HDR_MISO_0_P3: P3.6, R225.1
- new net HDR_MISO_0_P4: P4.6, R226.1
- new net HDR_MISO_0_P5: P5.6, R227.1
- new net HDR_MISO_0_P6: P6.6, R228.1
- new net HDR_MISO_1_P10: P10.6, R232.1
- new net HDR_MISO_1_P11: P11.6, R233.1
- new net HDR_MISO_1_P12: P12.6, R234.1
- new net HDR_MISO_1_P7: P7.6, R229.1
- new net HDR_MISO_1_P8: P8.6, R230.1
- new net HDR_MISO_1_P9: P9.6, R231.1
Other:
- note added: "SI2302-TP Digikey SI2302-TPMSCT-ND LCSC C4748714 or ME2306D LCSC C165220"
- note removed: "SI2302-TP Digikey SI2302-TPMSCT-ND LCSC C4748714"

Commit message: Worked on 12-12 arena layout.
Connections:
- net PAN5V.CS_00_P1: now also U37.3; no longer U37.1
- net PAN5V.CS_00_P7: now also U61.3; no longer U61.1
- net PAN5V.CS_01_P1: now also U37.1; no longer U37.3
- net PAN5V.CS_01_P7: now also U61.1; no longer U61.3
- net PAN5V.CS_02_P1: now also U38.3; no longer U38.1
- net PAN5V.CS_02_P7: now also U62.3; no longer U62.1
- net PAN5V.CS_03_P1: now also U38.1; no longer U38.3
- net PAN5V.CS_03_P7: now also U62.1; no longer U62.3
- net PAN5V.CS_04_P1: now also U39.3; no longer U39.1
- net PAN5V.CS_04_P7: now also U63.3; no longer U63.1
- net PAN5V.CS_05_P2: now also U41.3; no longer U41.1
- net PAN5V.CS_05_P8: now also U65.3; no longer U65.1
- net PAN5V.CS_06_P2: now also U41.1; no longer U41.3
- net PAN5V.CS_06_P8: now also U65.1; no longer U65.3
- net PAN5V.CS_07_P2: now also U42.3; no longer U42.1
- net PAN5V.CS_07_P8: now also U66.3; no longer U66.1
- net PAN5V.CS_08_P2: now also U42.1; no longer U42.3
- net PAN5V.CS_08_P8: now also U66.1; no longer U66.3
- net PAN5V.CS_09_P2: now also U43.3; no longer U43.1
- net PAN5V.CS_09_P8: now also U67.3; no longer U67.1
- net PAN5V.CS_10_P3: now also U45.3; no longer U45.1
- net PAN5V.CS_10_P9: now also U69.3; no longer U69.1
- net PAN5V.CS_11_P3: now also U45.1; no longer U45.3
- net PAN5V.CS_11_P9: now also U69.1; no longer U69.3
- net PAN5V.CS_12_P3: now also U46.3; no longer U46.1
- net PAN5V.CS_12_P9: now also U70.3; no longer U70.1
- net PAN5V.CS_13_P3: now also U46.1; no longer U46.3
- net PAN5V.CS_13_P9: now also U70.1; no longer U70.3
- net PAN5V.CS_14_P3: now also U47.3; no longer U47.1
- net PAN5V.CS_14_P9: now also U71.3; no longer U71.1
- net PAN5V.CS_15_P10: now also U73.3; no longer U73.1
- net PAN5V.CS_15_P4: now also U49.3; no longer U49.1
- net PAN5V.CS_16_P10: now also U73.1; no longer U73.3
- net PAN5V.CS_16_P4: now also U49.1; no longer U49.3
- net PAN5V.CS_17_P10: now also U74.3; no longer U74.1
- net PAN5V.CS_17_P4: now also U50.3; no longer U50.1
- net PAN5V.CS_18_P10: now also U74.1; no longer U74.3
- net PAN5V.CS_18_P4: now also U50.1; no longer U50.3
- net PAN5V.CS_19_P10: now also U75.3; no longer U75.1
- net PAN5V.CS_19_P4: now also U51.3; no longer U51.1
- net PAN5V.CS_20_P11: now also U77.3; no longer U77.1
- net PAN5V.CS_20_P5: now also U53.3; no longer U53.1
- net PAN5V.CS_21_P11: now also U77.1; no longer U77.3
- net PAN5V.CS_21_P5: now also U53.1; no longer U53.3
- net PAN5V.CS_22_P11: now also U78.3; no longer U78.1
- net PAN5V.CS_22_P5: now also U54.3; no longer U54.1
- net PAN5V.CS_23_P11: now also U78.1; no longer U78.3
- net PAN5V.CS_23_P5: now also U54.1; no longer U54.3
- net PAN5V.CS_24_P11: now also U79.3; no longer U79.1
- net PAN5V.CS_24_P5: now also U55.3; no longer U55.1
- net PAN5V.CS_25_P12: now also U81.3; no longer U81.1
- net PAN5V.CS_25_P6: now also U57.3; no longer U57.1
- net PAN5V.CS_26_P12: now also U81.1; no longer U81.3
- net PAN5V.CS_26_P6: now also U57.1; no longer U57.3
- net PAN5V.CS_27_P12: now also U82.3; no longer U82.1
- net PAN5V.CS_27_P6: now also U58.3; no longer U58.1
- net PAN5V.CS_28_P12: now also U82.1; no longer U82.3
- net PAN5V.CS_28_P6: now also U58.1; no longer U58.3
- net PAN5V.CS_29_P12: now also U83.3; no longer U83.1
- net PAN5V.CS_29_P6: now also U59.3; no longer U59.1
- net PAN5V.EXT_INT: now also U39.1, U43.1, U47.1, U51.1, U55.1, U59.1, U63.1, U67.1, U71.1, U75.1, U79.1, U83.1; no longer U39.3, U43.3, U47.3, U51.3, U55.3, U59.3, U63.3, U67.3, U71.3, U75.3, U79.3, U83.3
- net PAN5V.MOSI_0_P1: now also U36.1; no longer U36.3
- net PAN5V.MOSI_0_P2: now also U40.1; no longer U40.3
- net PAN5V.MOSI_0_P3: now also U44.1; no longer U44.3
- net PAN5V.MOSI_0_P4: now also U48.1; no longer U48.3
- net PAN5V.MOSI_0_P5: now also U52.1; no longer U52.3
- net PAN5V.MOSI_0_P6: now also U56.1; no longer U56.3
- net PAN5V.MOSI_1_P10: now also U72.1; no longer U72.3
- net PAN5V.MOSI_1_P11: now also U76.1; no longer U76.3
- net PAN5V.MOSI_1_P12: now also U80.1; no longer U80.3
- net PAN5V.MOSI_1_P7: now also U60.1; no longer U60.3
- net PAN5V.MOSI_1_P8: now also U64.1; no longer U64.3
- net PAN5V.MOSI_1_P9: now also U68.1; no longer U68.3
- net PAN5V.SCK_0_P1: now also U36.3; no longer U36.1
- net PAN5V.SCK_0_P2: now also U40.3; no longer U40.1
- net PAN5V.SCK_0_P3: now also U44.3; no longer U44.1
- net PAN5V.SCK_0_P4: now also U48.3; no longer U48.1
- net PAN5V.SCK_0_P5: now also U52.3; no longer U52.1
- net PAN5V.SCK_0_P6: now also U56.3; no longer U56.1
- net PAN5V.SCK_1_P10: now also U72.3; no longer U72.1
- net PAN5V.SCK_1_P11: now also U76.3; no longer U76.1
- net PAN5V.SCK_1_P12: now also U80.3; no longer U80.1
- net PAN5V.SCK_1_P7: now also U60.3; no longer U60.1
- net PAN5V.SCK_1_P8: now also U64.3; no longer U64.1
- net PAN5V.SCK_1_P9: now also U68.3; no longer U68.1
- net at U67.6: now also R190.2; no longer R189.2
- net at R195.2: now also U70.4; no longer U70.6
- net at R200.2: now also U72.6; no longer U72.4
- net at R140.2: now also U42.6; no longer U42.4
- net at U55.6: now also R166.2; no longer R165.2
- net at R139.2: now also U42.4; no longer U42.6
- net at U54.4: now also R163.2; no longer R164.2
- net at U38.6: now also R132.2; no longer R131.2
- net at U66.4: now also R187.2; no longer R188.2
- net at U57.6: now also R170.2; no longer R169.2
- net at R152.2: now also U48.6; no longer U48.4
- net at R217.2: now also U81.4; no longer U81.6
- net at U37.6: now also R130.2; no longer R129.2
- net at R220.2: now also U82.6; no longer U82.4
- net at R218.2: now also U81.6; no longer U81.4
- net at U50.6: now also R156.2; no longer R155.2
- net at U62.4: now also R179.2; no longer R180.2
- net at R201.2: now also U73.4; no longer U73.6
- net at R213.2: now also U79.4; no longer U79.6
- net at R196.2: now also U70.6; no longer U70.4
- net at U69.4: now also R193.2; no longer R194.2
- net at R185.2: now also U65.4; no longer U65.6
- net at R181.2: now also U63.4; no longer U63.6
- net at R168.2: now also U56.6; no longer U56.4
- net at R183.2: now also U64.4; no longer U64.6
- net at U78.4: now also R211.2; no longer R212.2
- net at R133.2: now also U39.4; no longer U39.6
- net at U52.6: now also R160.2; no longer R159.2
- net at R127.2: now also U36.4; no longer U36.6
- net at U62.6: now also R180.2; no longer R179.2
- net at R138.2: now also U41.6; no longer U41.4
- net at U78.6: now also R212.2; no longer R211.2
- net at U61.6: now also R178.2; no longer R177.2
- net at R182.2: now also U63.6; no longer U63.4
- net at U37.4: now also R129.2; no longer R130.2
- net at U40.4: now also R135.2; no longer R136.2
- net at U54.6: now also R164.2; no longer R163.2
- net at U71.6: now also R198.2; no longer R197.2
- net at U66.6: now also R188.2; no longer R187.2
- net at R148.2: now also U46.6; no longer U46.4
- net at R208.2: now also U76.6; no longer U76.4
- net at R214.2: now also U79.6; no longer U79.4
- net at U71.4: now also R197.2; no longer R198.2
- net at R142.2: now also U43.6; no longer U43.4
- net at R192.2: now also U68.6; no longer U68.4
- net at U38.4: now also R131.2; no longer R132.2
- net at U61.4: now also R177.2; no longer R178.2
- net at U60.6: now also R176.2; no longer R175.2
- net at R145.2: now also U45.4; no longer U45.6
- net at U83.4: now also R221.2; no longer R222.2
- net at R141.2: now also U43.4; no longer U43.6
- net at R173.2: now also U59.4; no longer U59.6
- net at U51.6: now also R158.2; no longer R157.2
- net at U57.4: now also R169.2; no longer R170.2
- net at U51.4: now also R157.2; no longer R158.2
- net at R215.2: now also U80.4; no longer U80.6
- net at U74.4: now also R203.2; no longer R204.2
- net at R134.2: now also U39.6; no longer U39.4
- net at U44.6: now also R144.2; no longer R143.2
- net at R202.2: now also U73.6; no longer U73.4
- net at U60.4: now also R175.2; no longer R176.2
- net at R174.2: now also U59.6; no longer U59.4
- net at R128.2: now also U36.6; no longer U36.4
- net at U83.6: now also R222.2; no longer R221.2
- net at U74.6: now also R204.2; no longer R203.2
- net at U40.6: now also R136.2; no longer R135.2
- net at R216.2: now also U80.6; no longer U80.4
- net at U53.6: now also R162.2; no longer R161.2
- net at U77.6: now also R210.2; no longer R209.2
- net at R171.2: now also U58.4; no longer U58.6
- net at U75.6: now also R206.2; no longer R205.2
- net at U75.4: now also R205.2; no longer R206.2
- net at U47.4: now also R149.2; no longer R150.2
- net at U77.4: now also R209.2; no longer R210.2
- net at U53.4: now also R161.2; no longer R162.2
- net at R167.2: now also U56.4; no longer U56.6
- net at R219.2: now also U82.4; no longer U82.6
- net at U55.4: now also R165.2; no longer R166.2
- net at R153.2: now also U49.4; no longer U49.6
- net at R154.2: now also U49.6; no longer U49.4
- net at R147.2: now also U46.4; no longer U46.6
- net at R172.2: now also U58.6; no longer U58.4
- net at R137.2: now also U41.4; no longer U41.6
- net at R191.2: now also U68.4; no longer U68.6
- net at R207.2: now also U76.4; no longer U76.6
- net at U47.6: now also R150.2; no longer R149.2
- net at U67.4: now also R189.2; no longer R190.2
- net at R151.2: now also U48.4; no longer U48.6
- net at R146.2: now also U45.6; no longer U45.4
- net at U52.4: now also R159.2; no longer R160.2
- net at U69.6: now also R194.2; no longer R193.2
- net at R184.2: now also U64.6; no longer U64.4
- net at U44.4: now also R143.2; no longer R144.2
- net at R186.2: now also U65.6; no longer U65.4
- net at U50.4: now also R155.2; no longer R156.2
- net at R199.2: now also U72.4; no longer U72.6
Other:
- moved on the sheet: U36A, U36B, U37A, U37B, U38A, U38B, U39A, U39B, U40A, U40B, U41A, U41B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

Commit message: Finished preliminary layout for new 12-12 teensy 4.1 arena.
Includes source termination resistors and schmitt trigger buffers.
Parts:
- C47, C48, C49, C50, C51, C52, C53, C54, C55, C56, C57, C58, C59, C60, C61, C62, C63, C64, C65, C66, C67, C68, C69, C70, C71, C72, C73, C74, C75, C76, C77, C78, C79, C80, C81, C82, C83, C84, C85, C86, C87, C88, C89, C90, C91, C92, C93, C94: footprint Capacitor_SMD:C_0603_1608Metric -> Capacitor_SMD:C_0402_1005Metric
- R127, R128, R129, R130, R131, R132, R133, R134, R135, R136, R137, R138, R139, R140, R141, R142, R143, R144, R145, R146, R147, R148, R149, R150, R151, R152, R153, R154, R155, R156, R157, R158, R159, R160, R161, R162, R163, R164, R165, R166, R167, R168, R169, R170, R171, R172, R173, R174, R175, R176, R177, R178, R179, R180, R181, R182, R183, R184, R185, R186, R187, R188, R189, R190, R191, R192, R193, R194, R195, R196, R197, R198, R199, R200, R201, R202, R203, R204, R205, R206, R207, R208, R209, R210, R211, R212, R213, R214, R215, R216, R217, R218, R219, R220, R221, R222, R223, R224, R225, R226, R227, R228, R229, R230, R231, R232, R233, R234: footprint Resistor_SMD:R_0603_1608Metric -> Resistor_SMD:R_0402_1005Metric
